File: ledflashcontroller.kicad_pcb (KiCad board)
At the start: 2 copper layers, 100 x 100 mm, 72 parts, among them J1 Conn_02x08_Odd_Even, J2 CONN_01X02, J3 CONN_01X02, J4 Conn_01x02, K1 LDD-1000H, K2 LDD-1000H, P1 V_IN, P10 BNC, P11 BNC, P12 BNC, P2 I2C_HEADER, P3 GPIO_HEADER, P4 V_DIM1, P5 V_DIM2, P6 V_OUT, P7 BNC, P8 BNC, P9 BNC, Q1 IRLML6244, Q2 IRFB3256, U1 Teensy3.6, U10 DMC2700, U11 DS3231, U2 ISO1540, U3 DMC2700, U4 DMC2700, U5 ISO1540, U6 DMC2700, U7 DMC2700, U8 ISO1540, U9 DMC2700

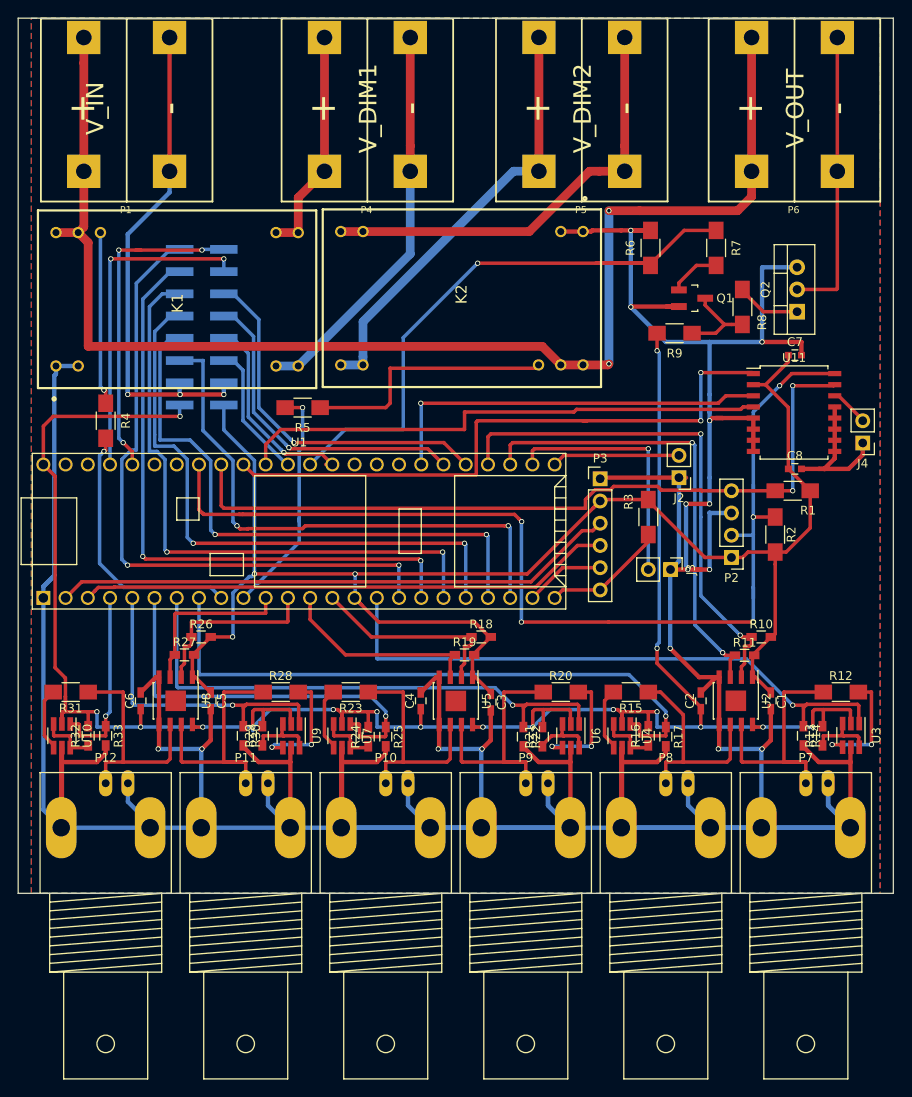
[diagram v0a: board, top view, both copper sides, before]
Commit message: fixed decoupling cap for U8
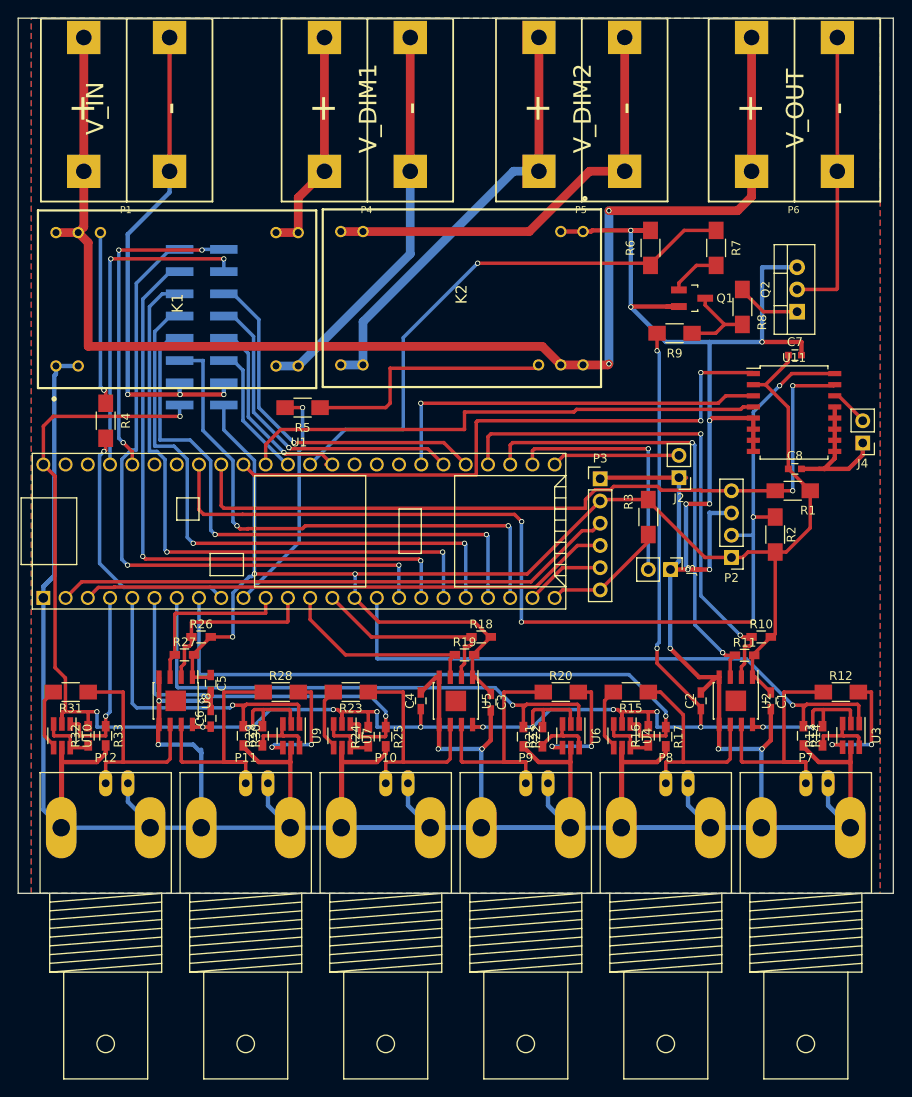
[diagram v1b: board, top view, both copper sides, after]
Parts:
- moved C6 8.25 mm to (52.0, 110.0)
- moved C5 2.00 mm to (52.0, 106.0)
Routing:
- net /VOUT: track 69.9 -> 63.9 mm
- net /SCL: track 124.8 -> 120.7 mm
- net +3V3: track 184.8 -> 181.8 mm
- net +5V: track 242.5 -> 240.5 mm, vias 17 -> 16
- net /TRIG_IO1: track 37.7 -> 37.2 mm
- net GND: track 693.0 -> 692.5 mm, vias 18 -> 19
- net /RTC_32kHz: track 70.9 -> 70.4 mm

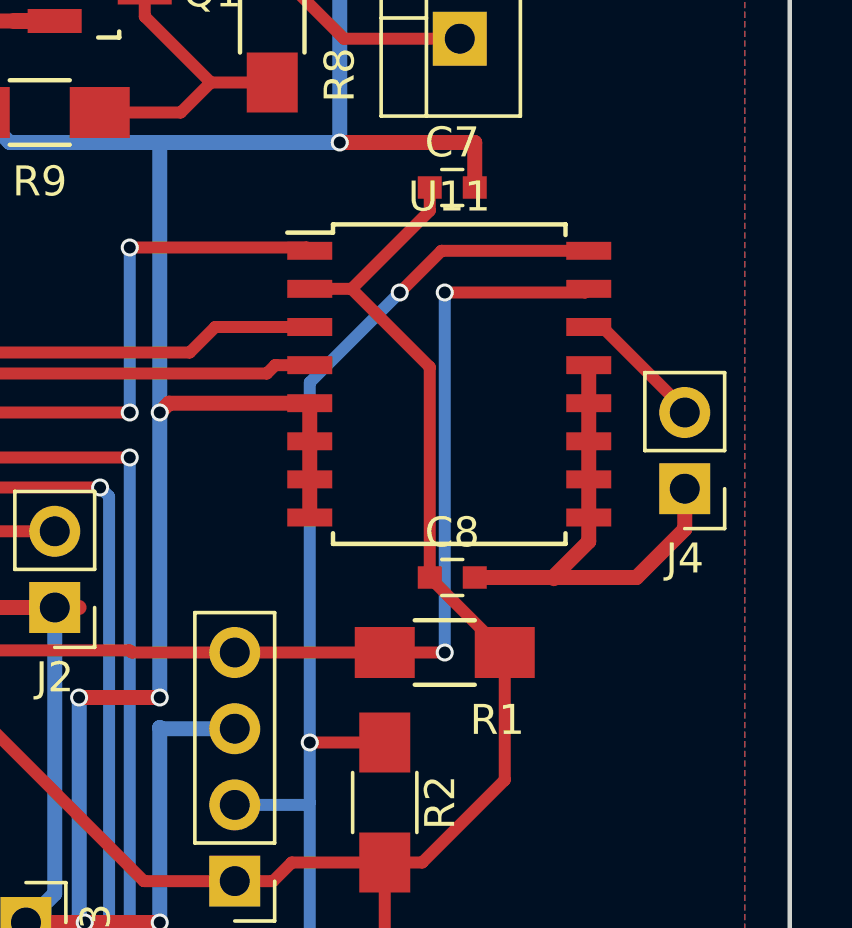
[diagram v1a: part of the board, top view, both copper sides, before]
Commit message: fixed decoupling cap for U11
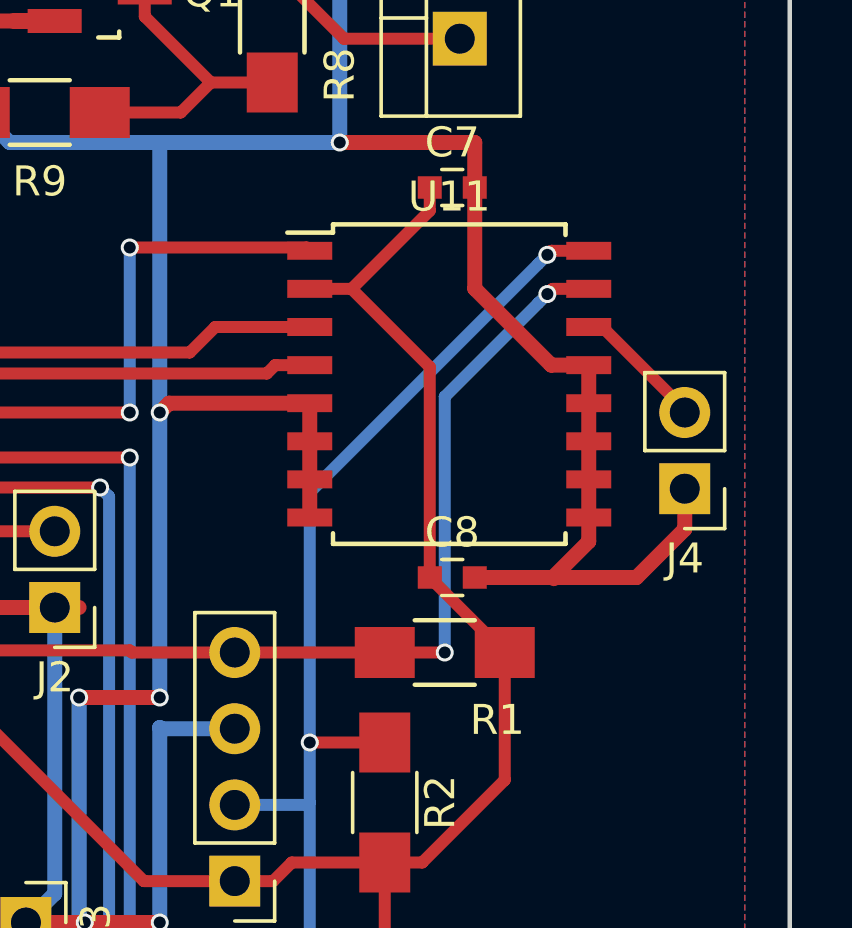
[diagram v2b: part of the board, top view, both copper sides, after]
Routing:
- net GND: track 692.5 -> 700.8 mm
- net /SCL: track 120.7 -> 118.6 mm
- net /SDA: track 88.8 -> 86.8 mm
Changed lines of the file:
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@@
     (thickness 1.6)
     (drawings 8)
-    (tracks 943)
+    (tracks 949)
     (zones 0)
     (modules 72)
@@
   (segment (start 38 109.25) (end 38 110.9) (width 0.4) (layer F.Cu) (net 1) (status 20))
   (segment (start 35 109.25) (end 38 109.25) (width 0.4) (layer F.Cu) (net 1))
+  (segment (start 119.5 68.5) (end 119.5 71.87) (width 0.5) (layer F.Cu) (net 2))
+  (segment (start 119.5 71.87) (end 122.05 74.42) (width 0.5) (layer F.Cu) (net 2))
+  (segment (start 122.05 74.42) (end 123.3 74.42) (width 0.5) (layer F.Cu) (net 2))
   (segment (start 46.095 108) (end 46.095 105.3) (width 0.5) (layer F.Cu) (net 2) (status 20))
   (segment (start 46.095 110.7) (end 46.095 108) (width 0.5) (layer F.Cu) (net 2) (status 10))
@@
   (segment (start 49.905 105.3) (end 49.905 102.945) (width 0.4) (layer F.Cu) (net 9) (status 30))
   (segment (start 49.905 102.945) (end 50.1 102.75) (width 0.4) (layer F.Cu) (net 9) (status 30))
+  (segment (start 122.055207 70.61) (end 121.920646 70.744561) (width 0.4) (layer F.Cu) (net 10))
+  (segment (start 123.3 70.61) (end 122.055207 70.61) (width 0.4) (layer F.Cu) (net 10))
+  (segment (start 121.620647 71.04456) (end 121.920646 70.744561) (width 0.4) (layer B.Cu) (net 10))
+  (segment (start 114 87) (end 114 78.665207) (width 0.4) (layer B.Cu) (net 10))
+  (segment (start 114 78.665207) (end 121.620647 71.04456) (width 0.4) (layer B.Cu) (net 10))
+  (via (at 121.920646 70.744561) (size 0.6) (drill 0.4) (layers F.Cu B.Cu) (net 10))
   (segment (start 114 89) (end 114 99) (width 0.4) (layer B.Cu) (net 10))
   (segment (start 87.5 99) (end 114 99) (width 0.4) (layer F.Cu) (net 10))
@@
   (segment (start 87.5 87.554859) (end 87.532313 87.522546) (width 0.4) (layer B.Cu) (net 10))
   (via (at 87.532313 87.522546) (size 0.6) (drill 0.4) (layers F.Cu B.Cu) (net 10))
-  (segment (start 114 87) (end 114 75) (width 0.4) (layer B.Cu) (net 10))
-  (segment (start 117 72) (end 114 75) (width 0.4) (layer B.Cu) (net 10))
-  (segment (start 123.3 70.61) (end 118.39 70.61) (width 0.4) (layer F.Cu) (net 10) (status 10))
-  (segment (start 118.39 70.61) (end 117 72) (width 0.4) (layer F.Cu) (net 10))
-  (via (at 117 72) (size 0.6) (drill 0.4) (layers F.Cu B.Cu) (net 10))
   (segment (start 114 89) (end 114 87) (width 0.4) (layer B.Cu) (net 10))
   (segment (start 116.5 87) (end 114 87) (width 0.4) (layer F.Cu) (net 10) (status 10))
@@
   (segment (start 113.92 89.08) (end 114 89) (width 0.4) (layer B.Cu) (net 10))
   (via (at 87.5 99) (size 0.6) (drill 0.4) (layers F.Cu B.Cu) (net 10))
+  (segment (start 118.5 75.472215) (end 121.620647 72.351568) (width 0.4) (layer B.Cu) (net 11))
+  (segment (start 118.5 84) (end 118.5 75.472215) (width 0.4) (layer B.Cu) (net 11))
+  (segment (start 121.620647 72.351568) (end 121.920646 72.051569) (width 0.4) (layer B.Cu) (net 11))
+  (segment (start 122.092215 71.88) (end 121.920646 72.051569) (width 0.4) (layer F.Cu) (net 11))
+  (segment (start 123.3 71.88) (end 122.092215 71.88) (width 0.4) (layer F.Cu) (net 11))
+  (via (at 121.920646 72.051569) (size 0.6) (drill 0.4) (layers F.Cu B.Cu) (net 11))
   (segment (start 53.2 81) (end 53.2 85.7) (width 0.4) (layer F.Cu) (net 11) (status 10))
   (segment (start 53.2 85.7) (end 53.5 86) (width 0.4) (layer F.Cu) (net 11))
@@
   (segment (start 103.070002 83.5) (end 103.5 83.929998) (width 0.4) (layer F.Cu) (net 11))
   (segment (start 98.050002 83.5) (end 103.070002 83.5) (width 0.4) (layer F.Cu) (net 11))
-  (segment (start 118.5 72) (end 123.18 72) (width 0.4) (layer F.Cu) (net 11) (status 20))
-  (segment (start 123.18 72) (end 123.3 71.88) (width 0.4) (layer F.Cu) (net 11) (status 30))
-  (segment (start 118.5 84) (end 118.5 72) (width 0.4) (layer B.Cu) (net 11))
-  (via (at 118.5 72) (size 0.6) (drill 0.4) (layers F.Cu B.Cu) (net 11))
   (segment (start 116.5 84) (end 118.5 84) (width 0.4) (layer F.Cu) (net 11) (status 10))
   (via (at 118.5 84) (size 0.6) (drill 0.4) (layers F.Cu B.Cu) (net 11))

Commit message: Cleanups
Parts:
- U2, U5, U8: footprint Housings_SOIC:SOIC-8-1EP_3.9x4.9mm_Pitch1.27mm -> Housings_SOIC:SOIC-8_3.9x4.9mm_Pitch1.27mm
- moved R2 2.83 mm to (118.5, 87.0), turned to 0 degrees
- moved R6 0.75 mm to (102.2, 57.0)
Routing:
- net GND: track 700.8 -> 765.4 mm, vias 19 -> 13
- net /SCL: track 118.6 -> 100.4 mm, vias 5 -> 2
- net /TRIG_PU10: track 68.0 -> 64.5 mm
- net /TRIG_IO9: track 59.8 -> 57.1 mm
- net +48V: track 152.6 -> 150.5 mm
- net /RTC_SQW: track 45.5 -> 43.5 mm
- net Net-(P6-Pad2): track 33.3 -> 31.4 mm
- net /RTC_RST: track 61.2 -> 59.3 mm
- net /TRIG_PU8: track 71.3 -> 69.6 mm
- net /RTC_32kHz: track 70.4 -> 68.8 mm
- net /TRIG_PU9: track 68.2 -> 66.7 mm
- net /TRIG_IO8: track 53.3 -> 51.8 mm
- net Net-(K1-Pad22): track 19.8 -> 21.2 mm
- net /TRIG_PU11: track 63.9 -> 62.5 mm
- net /SDA: track 86.8 -> 88.1 mm
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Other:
- net class GND removed

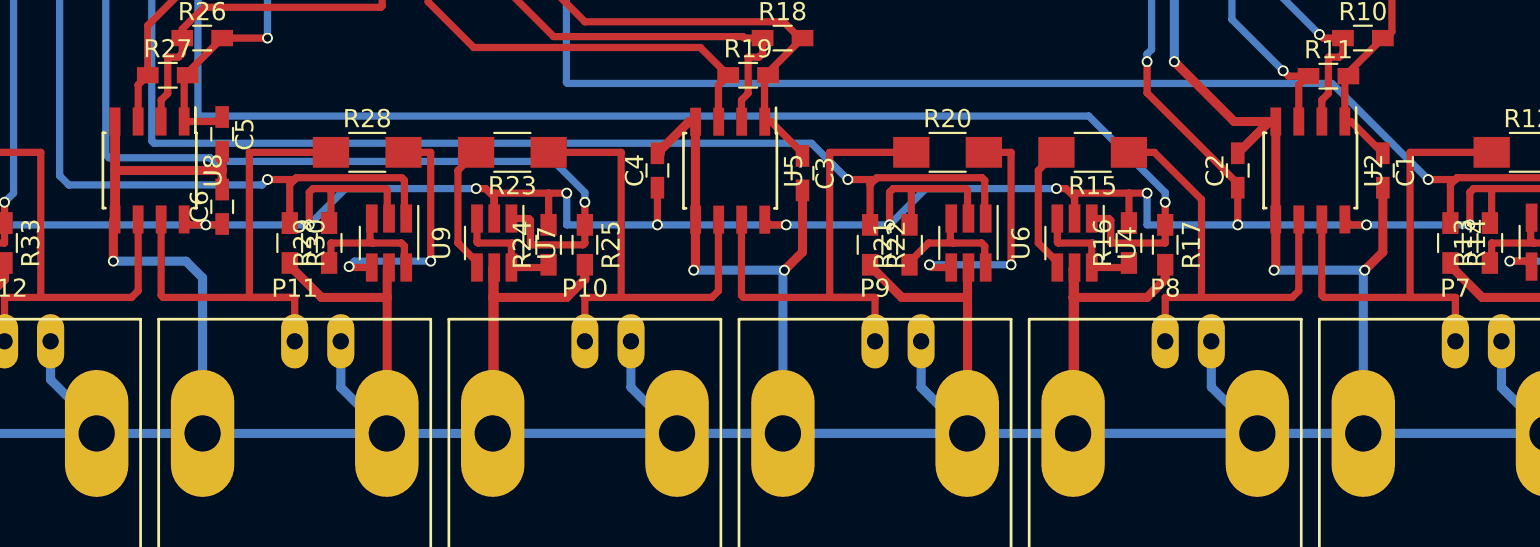
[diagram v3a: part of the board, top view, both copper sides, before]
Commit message: Fixed ISO1540 decoupling issue
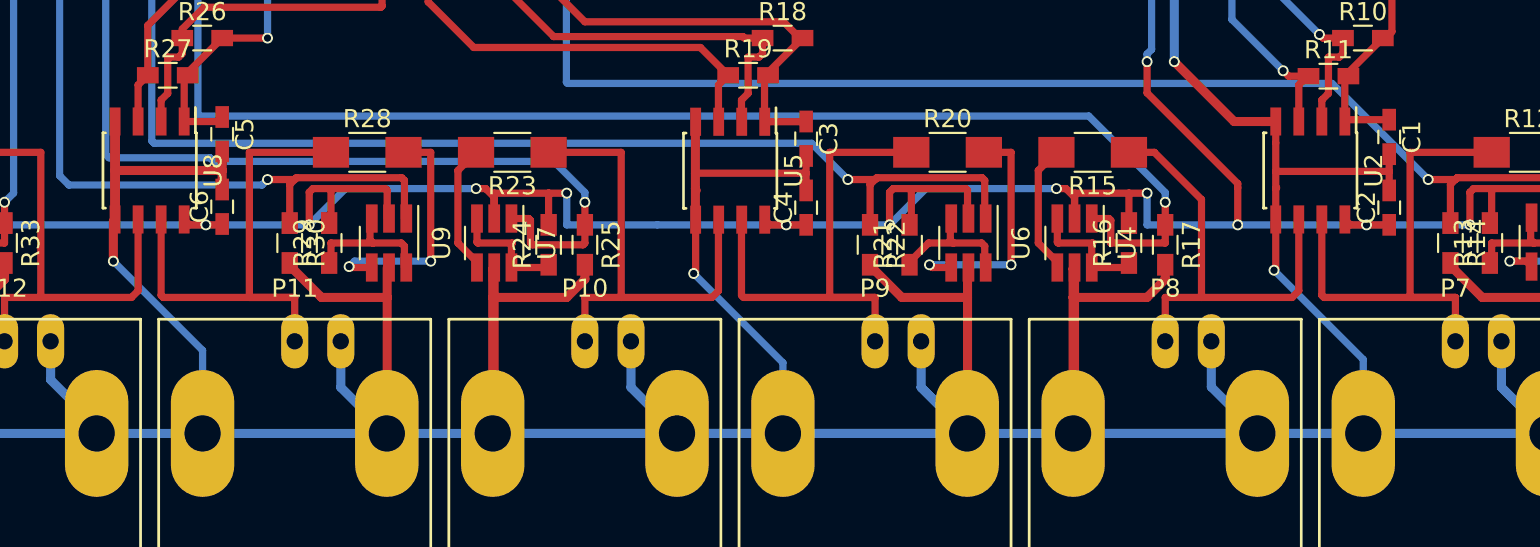
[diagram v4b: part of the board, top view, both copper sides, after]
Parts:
- moved C2 8.60 mm to (116.3, 110.0)
- moved C4 8.45 mm to (84.2, 110.0)
- moved C3 1.91 mm to (84.2, 106.2)
- moved C1 1.88 mm to (116.3, 106.2)
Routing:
- net GND: track 765.4 -> 757.4 mm, vias 13 -> 11
- net +3V3: track 181.1 -> 180.6 mm
- net +5V: track 240.5 -> 240.8 mm, vias 16 -> 15

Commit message: Cleanup teensy schematic and remove old custom.lib
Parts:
- U1: value Teensy3.6 -> Teensy3.6_no-center; footprint lib_fp:Teensy35_36_no_center -> lib_fp:Teensy35_36_no-center

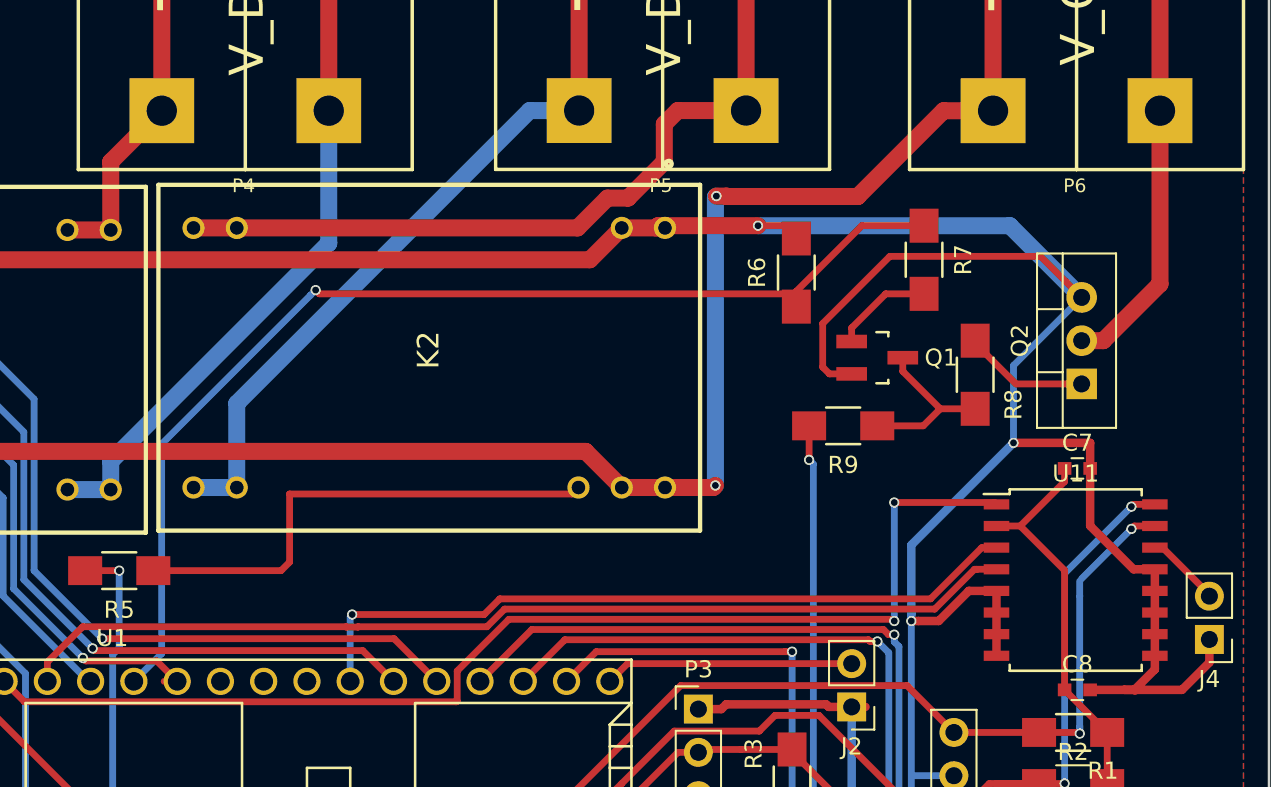
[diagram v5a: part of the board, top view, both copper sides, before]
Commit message: Add 2nd teensy ground and rotate mosfet. Fixes #3
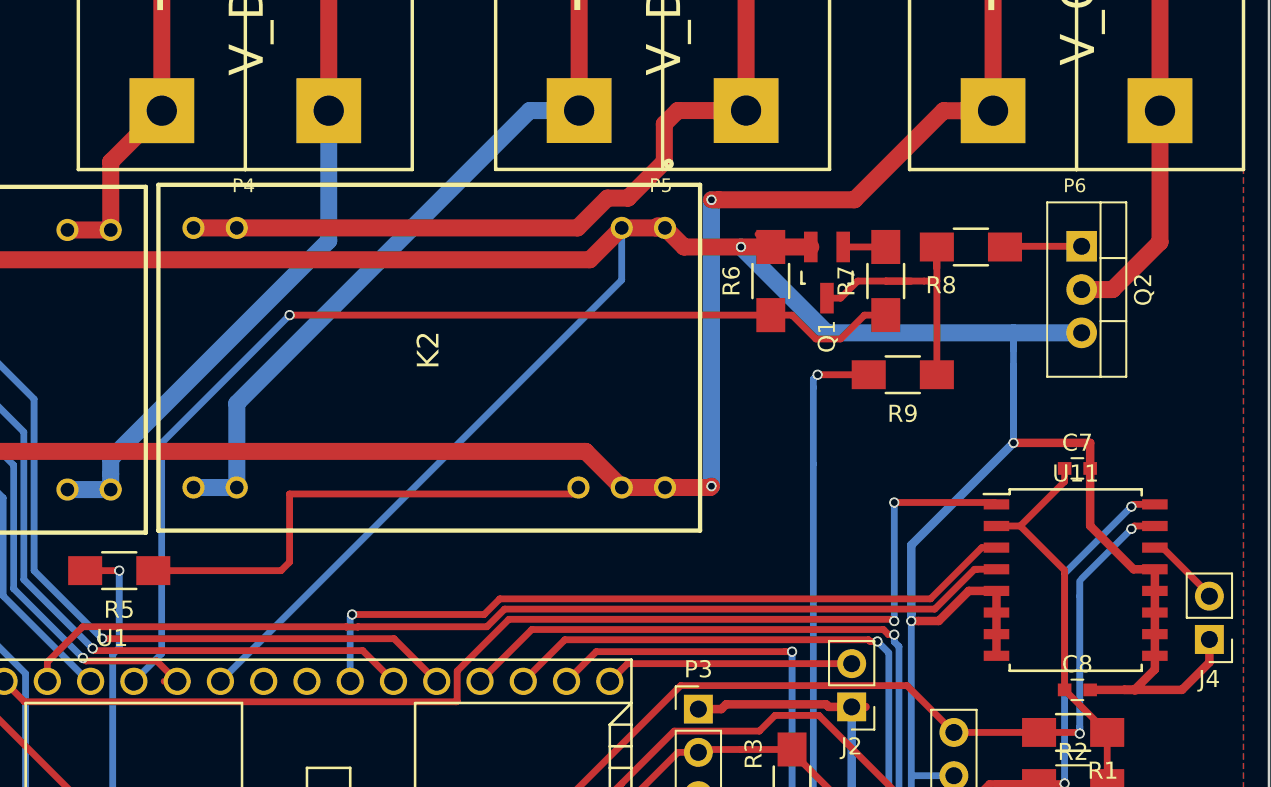
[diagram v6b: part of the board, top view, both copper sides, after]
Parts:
- moved Q2 8.08 mm to (119.0, 55.5), turned to 270 degrees
- moved R8 7.50 mm to (112.5, 55.5), turned to 0 degrees
- moved Q1 5.80 mm to (104.0, 57.0), turned to 180 degrees
- moved R9 4.61 mm to (108.5, 63.0)
- moved R7 2.57 mm to (107.5, 57.5), turned to 90 degrees
- moved R6 1.58 mm to (100.8, 57.5)
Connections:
- U1 pad 39: (no net) -> GND
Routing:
- net GND: track 757.4 -> 770.3 mm
- net Net-(Q1-Pad3): track 10.2 -> 17.1 mm
- net +5V: track 240.8 -> 246.8 mm
- net /VOUT: track 64.9 -> 61.4 mm
- net Net-(Q1-Pad1): track 5.88 -> 2.50 mm
- net Net-(Q2-Pad1): track 7.39 -> 4.52 mm
- net Net-(P6-Pad2): track 31.4 -> 28.8 mm
